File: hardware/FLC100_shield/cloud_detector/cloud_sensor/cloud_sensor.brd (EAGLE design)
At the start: 22.9 x 49.5 mm, 12 parts, among them IC1 MLX90614, Q1 2N7000, X1 SHIELD, X2 SENSOR

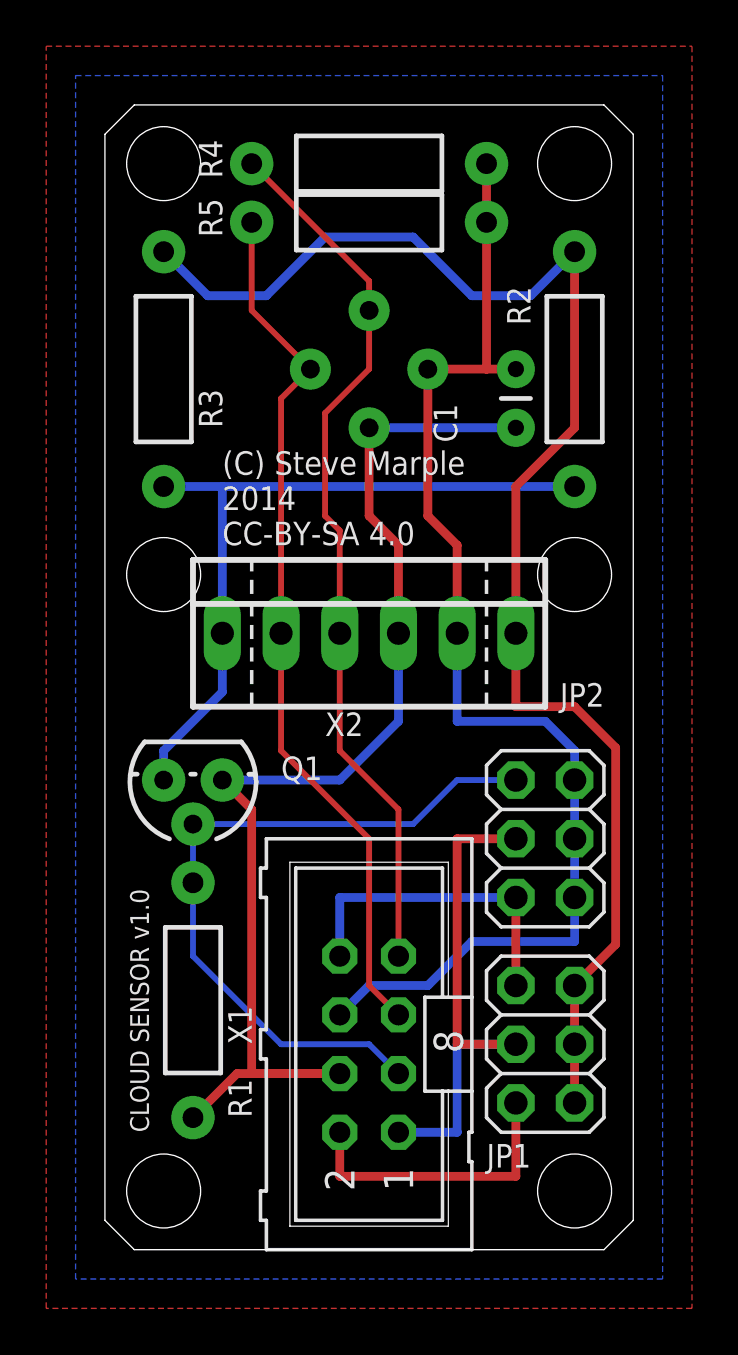
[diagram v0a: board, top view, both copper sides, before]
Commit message: Adding additional decoupling capacitor.
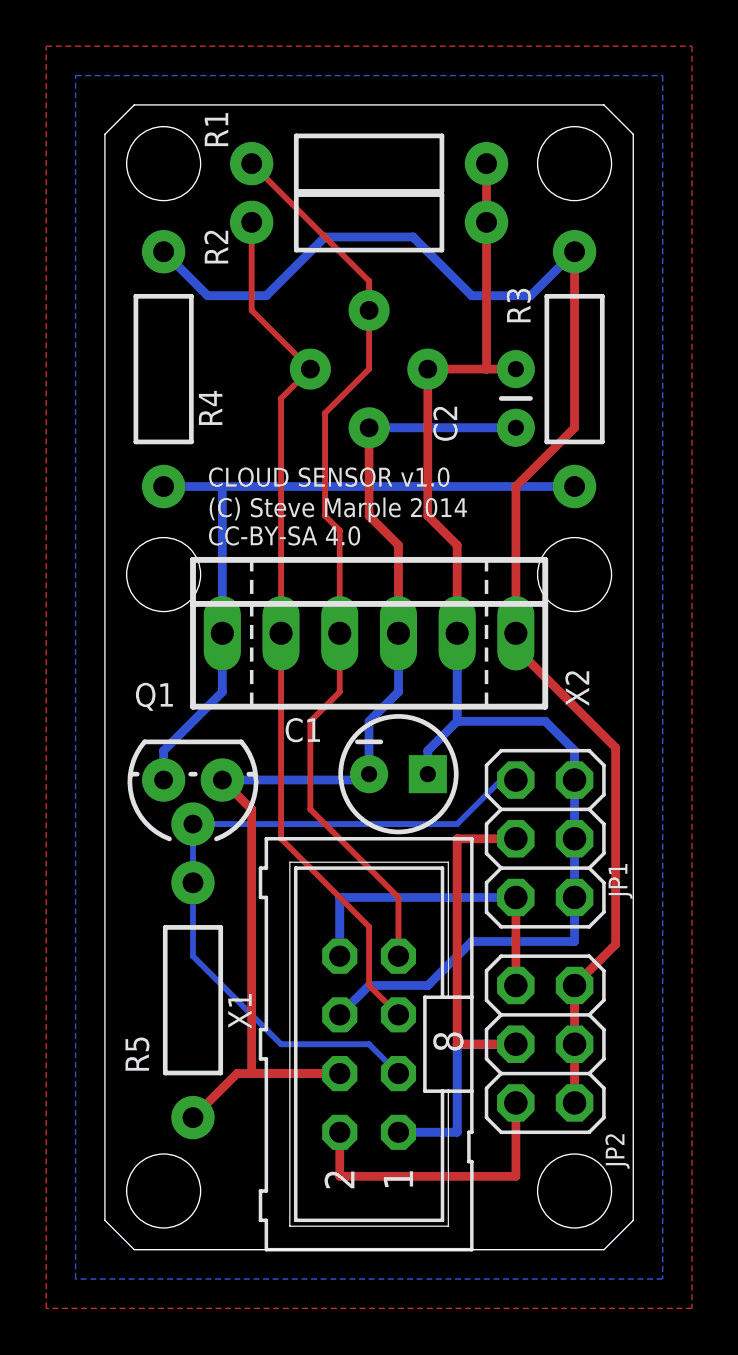
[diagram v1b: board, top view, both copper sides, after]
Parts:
- added C2: 100n, SparkFun:CAP-PTH-SMALL
- C1: value 100n -> 4u7; device SparkFun:CAP-PTH-SMALL -> SteveMarple:CPOL-RADIAL-10UF-25V
- JP1: value HEAT VCC -> VCC
- JP2: value VCC -> HEAT VCC
- R1: value 1M -> 10k
- R2: value 100R -> 10k
- R4: value 10k -> 100R
- R5: value 10k -> 1M
- moved R1 37.0 mm to (11.4, 47.0), turned to 0 degrees
- moved R5 34.5 mm to (3.81, 10.8), turned to 90 degrees
- moved C1 18.2 mm to (12.7, 20.6), turned to 0 degrees
- moved R3 17.8 mm to (20.3, 38.1)
- moved R4 12.6 mm to (2.54, 38.1), turned to 90 degrees
- moved R2 10.9 mm to (11.4, 44.5), turned to 0 degrees
- moved JP1 8.89 mm to (19.1, 17.8), turned to 90 degrees
- moved JP2 8.89 mm to (19.1, 8.89), turned to 270 degrees
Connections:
- net +3V3: now also JP1.2, JP2.1; no longer JP1.1, JP2.2
- net +5V: now also JP1.4, JP2.3; no longer JP1.3, JP2.4
- net CONTROL: now also JP1.6, R5.P$2; no longer JP2.6, R1.P$2
- net GND: now also C2.2, R5.P$1; no longer R1.P$1
- net HEATER_CONTROL: now also R4.P$1; no longer R2.P$1
- net HEATER_VCC: now also JP2.2, JP2.4, JP2.6, R4.P$2; no longer JP1.2, JP1.4, JP1.6, R2.P$2
- net SCL: now also R2.P$1; no longer R5.P$1
- net SDA: now also R1.P$1; no longer R4.P$1
- net VCC: now also C2.1, JP1.1, JP1.3, JP1.5, R1.P$2, R2.P$2; no longer JP2.1, JP2.3, JP2.5, R4.P$2, R5.P$2
- net VIN: now also JP2.5; no longer JP1.5
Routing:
- net VCC: track 53.8 -> 56.6 mm
- net HEATER_VCC: track 63.4 -> 61.9 mm
- net SDA: track 38.5 -> 39.6 mm
- net GND: track 52.4 -> 53.2 mm
